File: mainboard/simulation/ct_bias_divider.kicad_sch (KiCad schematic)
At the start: 23 parts

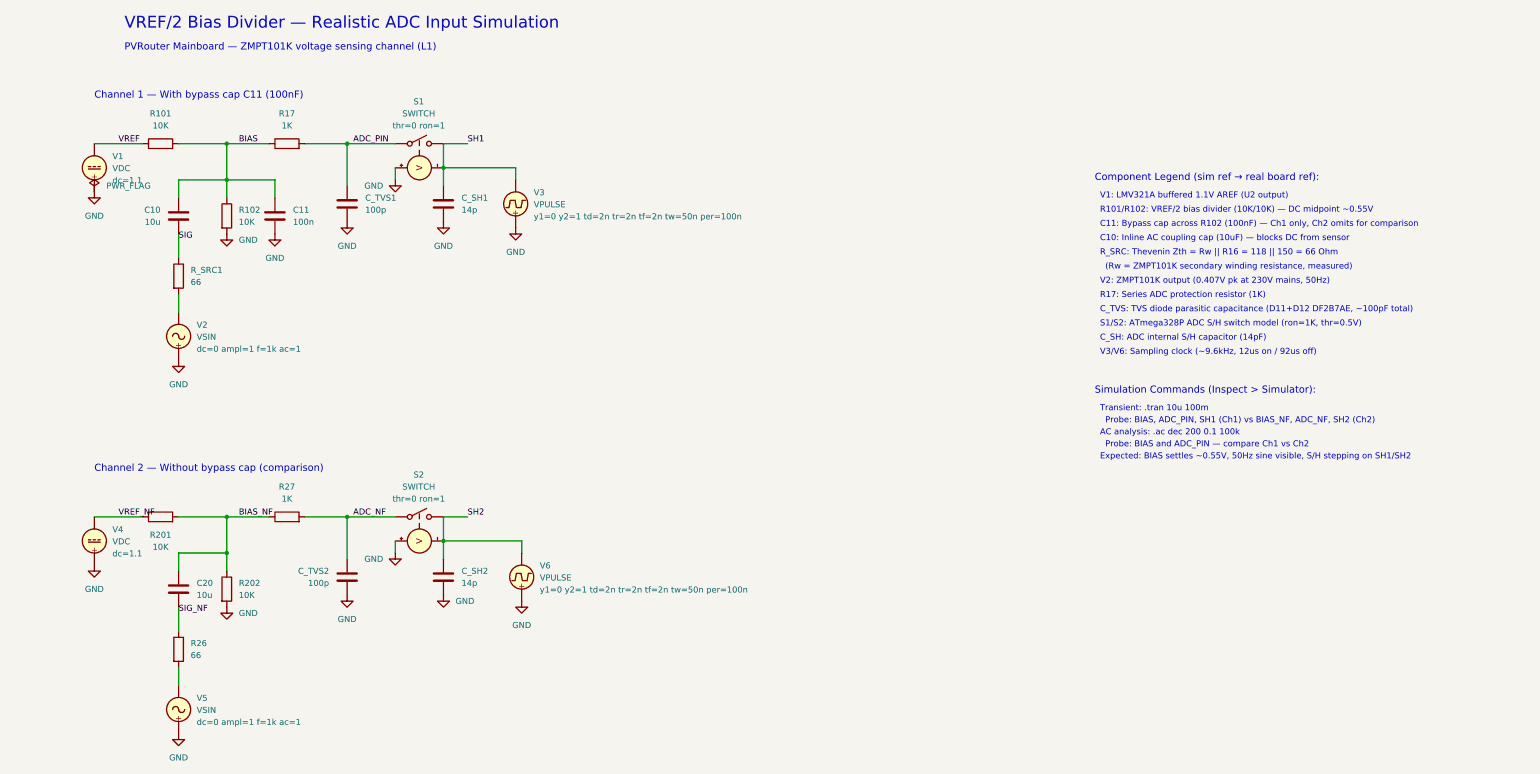
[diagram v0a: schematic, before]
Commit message: Add LCSC part numbers, MPC10-5 footprint, and simulation updates
- Add LCSC fields to mk2Wifi schematic (20 components for JLCPCB assembly)
- Add LCSC fields to mainboard schematic (18x 20K resistors, 12x 100nF caps)
- Add power indicator LED (LED40) and series resistor (R43) to mainboard
- Add MPC10-5 AC-DC converter custom footprint and TMF_05105 3D model
- Add CT and combined bias divider simulation schematics with generators
- Update mainboard PCB layout and bias divider simulation

Co-Authored-By: Claude Opus 4.6 <noreply@anthropic.com>
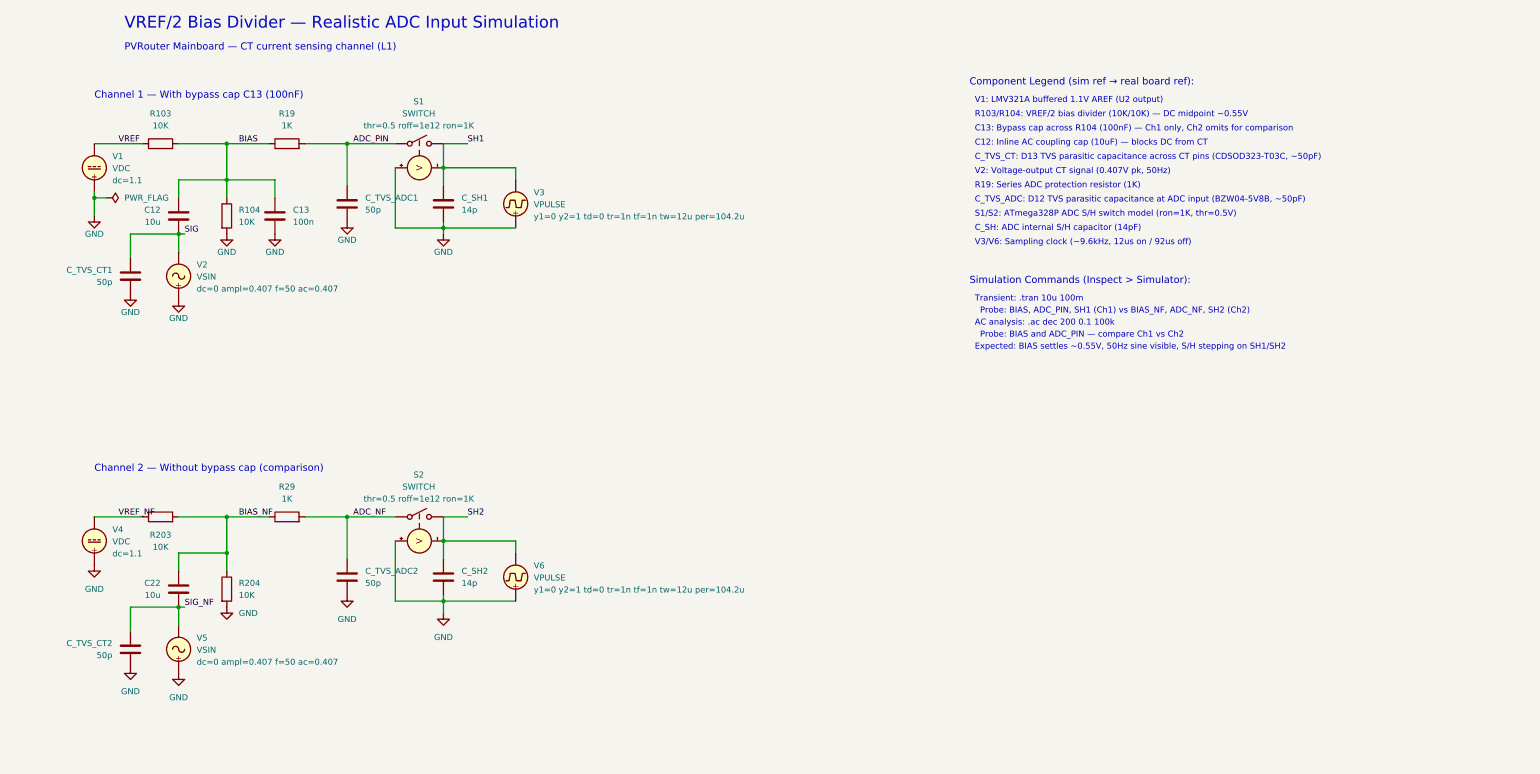
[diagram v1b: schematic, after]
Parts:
- removed C10, C20: 10u, symbol Device:C
- removed C11: 100n, symbol Device:C
- removed C_TVS1, C_TVS2: 100p, symbol Device:C
- removed R101, R102, R201, R202: 10K, symbol Device:R
- removed R17, R27: 1K, symbol Device:R
- removed R26, R_SRC1: 66, symbol Device:R
- added C12, C22: 10u, symbol Device:C
- added C13: 100n, symbol Device:C
- added C_TVS_ADC1, C_TVS_ADC2, C_TVS_CT1, C_TVS_CT2: 50p, symbol Device:C
- added R103, R104, R203, R204: 10K, symbol Device:R
- added R19, R29: 1K, symbol Device:R
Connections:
- net ADC_NF: now also C_TVS_ADC2.1, R29.2
- net ADC_PIN: now also C_TVS_ADC1.1, R19.2
- net BIAS: now also C12.1, C13.1, R103.2, R104.1, R19.1
- net BIAS_NF: now also C22.1, R203.2, R204.1, R29.1
- net GND: now also C13.2, C_TVS_ADC1.2, C_TVS_ADC2.2, C_TVS_CT1.2, C_TVS_CT2.2, R104.2, R204.2
- net SIG: now also V2.2, C12.2, C_TVS_CT1.1
- net SIG_NF: now also V5.2, C22.2, C_TVS_CT2.1
- net VREF: now also R103.1
- net VREF_NF: now also R203.1
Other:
- note added: "C12: Inline AC coupling cap (10uF) — blocks DC from CT"
- note added: "C13: Bypass cap across R104 (100nF) — Ch1 only, Ch2 omits for comparison"
- note added: "C_TVS_ADC: D12 TVS parasitic capacitance at ADC input (BZW04-5V8B, ~50pF)"
- note added: "C_TVS_CT: D13 TVS parasitic capacitance across CT pins (CDSOD323-T03C, ~50pF)"
- note added: "Channel 1 — With bypass cap C13 (100nF)"
- note added: "PVRouter Mainboard — CT current sensing channel (L1)"
- note added: "R103/R104: VREF/2 bias divider (10K/10K) — DC midpoint ~0.55V"
- note added: "R19: Series ADC protection resistor (1K)"
- note added: "V2: Voltage-output CT signal (0.407V pk, 50Hz)"
- note removed: "(Rw = ZMPT101K secondary winding resistance, measured)"
- note removed: "C10: Inline AC coupling cap (10uF) — blocks DC from sensor"
- note removed: "C11: Bypass cap across R102 (100nF) — Ch1 only, Ch2 omits for comparison"
- note removed: "C_TVS: TVS diode parasitic capacitance (D11+D12 DF2B7AE, ~100pF total)"
- note removed: "Channel 1 — With bypass cap C11 (100nF)"
- note removed: "PVRouter Mainboard — ZMPT101K voltage sensing channel (L1)"
- note removed: "R101/R102: VREF/2 bias divider (10K/10K) — DC midpoint ~0.55V"
- note removed: "R17: Series ADC protection resistor (1K)"
- note removed: "R_SRC: Thevenin Zth = Rw || R16 = 118 || 150 = 66 Ohm"
- note removed: "V2: ZMPT101K output (0.407V pk at 230V mains, 50Hz)"

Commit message: Fix dangling labels in CT bias divider simulation
Add stub wires from SIG/SIG_NF junctions to label positions
so ERC passes cleanly (0 violations).

Co-Authored-By: Claude Opus 4.6 <noreply@anthropic.com>
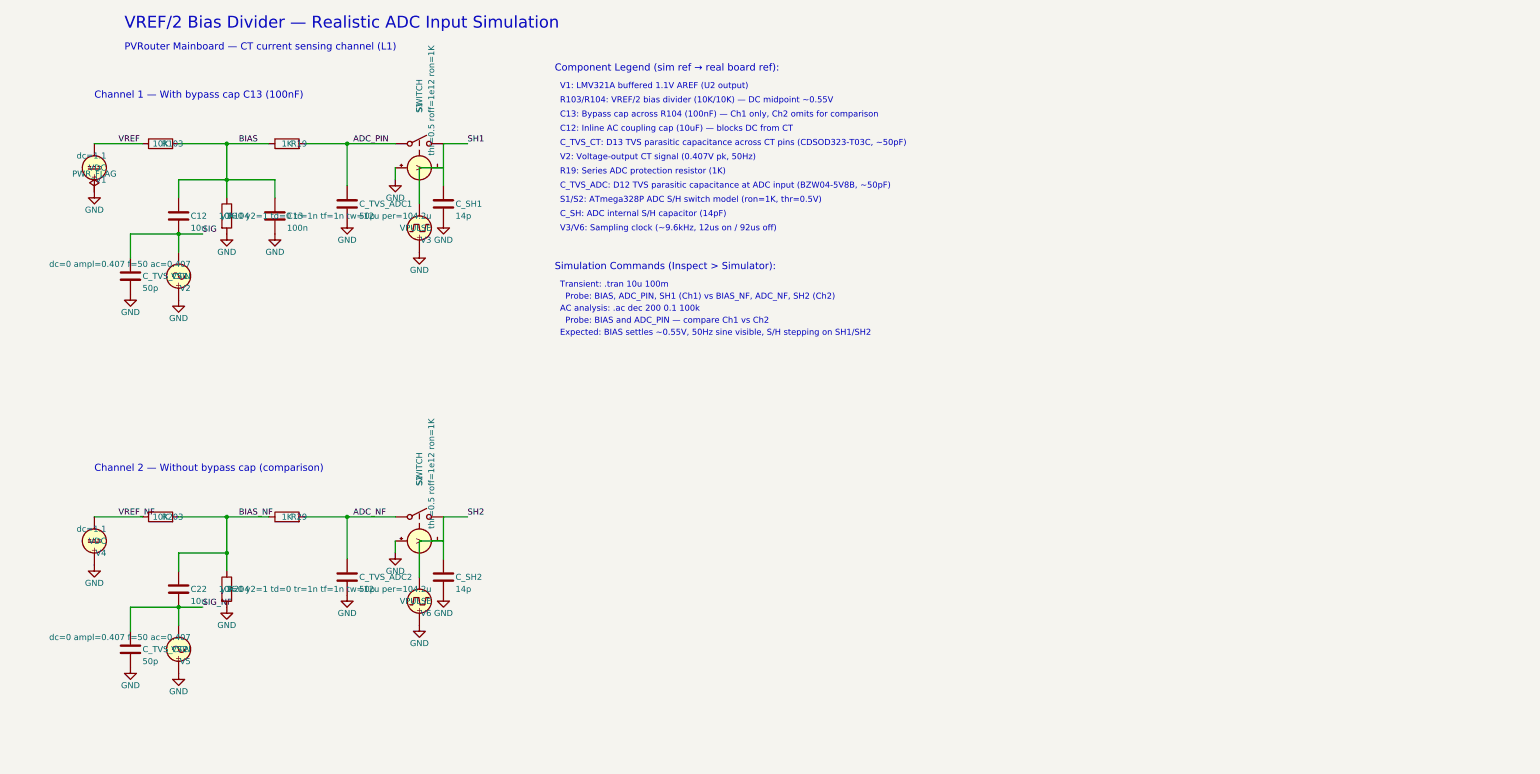
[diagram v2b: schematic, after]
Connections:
- net SH1: no longer S1.4 (C-), V3.2
- net SH2: no longer S2.4 (C-), V6.2
- new net: S1.4 (C-), V3.2
- new net: S2.4 (C-), V6.2
